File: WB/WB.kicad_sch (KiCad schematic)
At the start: 30 parts, among them J1 Conn_01x04, J2 Conn_01x04, J3 Conn_01x04, J4 Screw_Terminal_01x02, Q1 Q_NMOS_GDS, Q2 Q_NMOS_GDS, Q3 Q_NMOS_GDS, Q4 Q_NMOS_GDS, Q5 Q_NMOS_GDS, Q6 Q_NPN_ECB, SW1 SW_DIP_x06, U1 74HC165, U2 74HC595

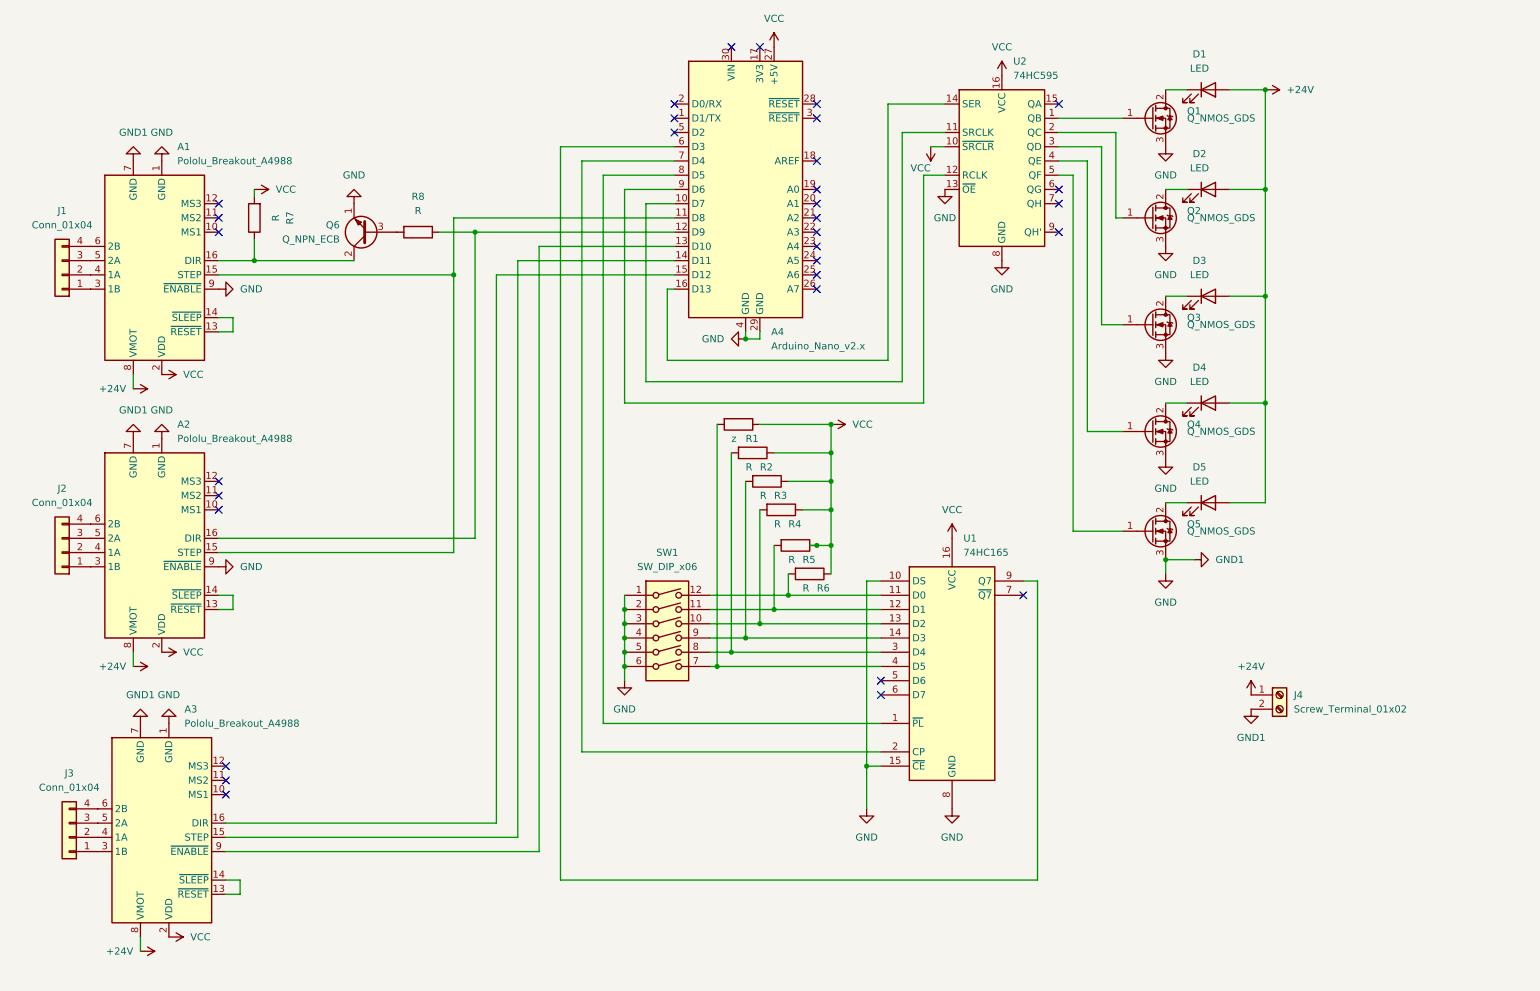
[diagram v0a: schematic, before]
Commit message: ファン、アクチュエーターを追加。配置を修正
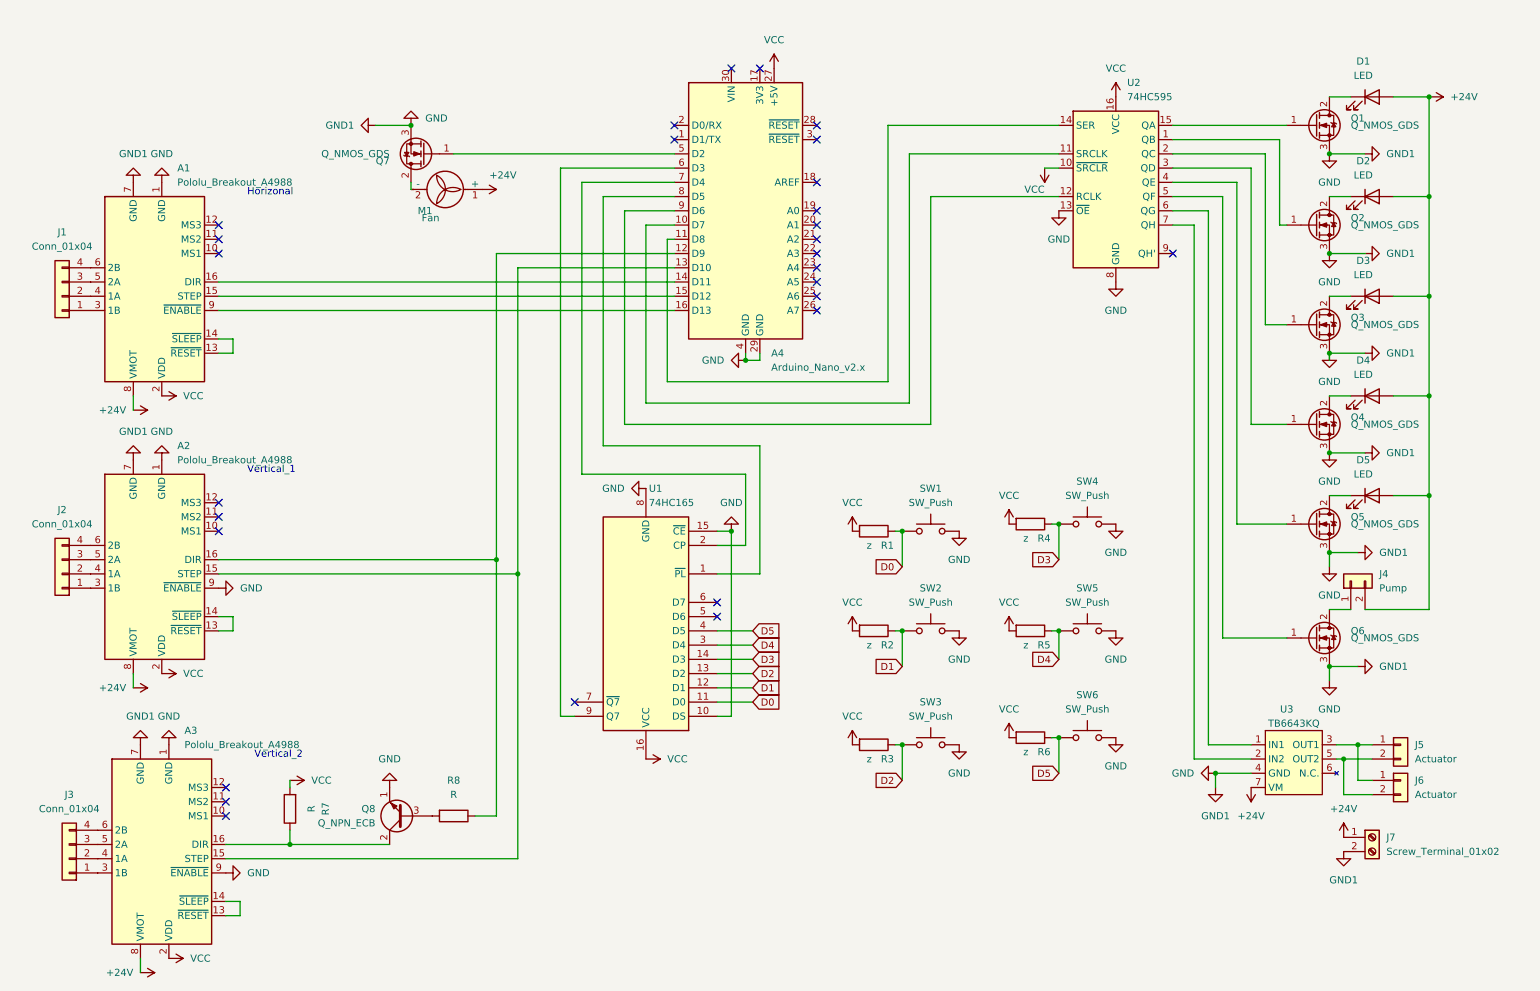
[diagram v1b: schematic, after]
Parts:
- removed Q6: Q_NPN_ECB, Package_TO_SOT_THT:TO-92_Inline, symbol Device:Q_NPN_ECB
- removed SW1: SW_DIP_x06, Connector_PinHeader_2.00mm:PinHeader_2x06_P2.00mm_Vertical, symbol Switch:SW_DIP_x06
- added J4: Pump, Connector_PinHeader_1.27mm:PinHeader_1x02_P1.27mm_Vertical, symbol Connector_Generic:Conn_01x02
- added J5, J6: Actuator, Connector_PinHeader_1.27mm:PinHeader_1x02_P1.27mm_Vertical, symbol Connector_Generic:Conn_01x02
- added M1: Fan, Connector_PinHeader_1.27mm:PinHeader_1x02_P1.27mm_Vertical, symbol Motor:Fan
- added Q6, Q7: Q_NMOS_GDS, 2sk2232:TO254P1054X470X1955-3, symbol Device:Q_NMOS_GDS
- added Q8: Q_NPN_ECB, Package_TO_SOT_THT:TO-92_Inline, symbol Device:Q_NPN_ECB
- added SW1, SW2, SW3, SW4, SW5, SW6: SW_Push, Connector_PinHeader_1.27mm:PinHeader_1x02_P1.27mm_Vertical, symbol Switch:SW_Push
- added U3: TB6643KQ, TB6643KQ:SIP1005W50P254L1965H1265Q7, symbol TB6643KQ:TB6643KQ
- D1, D2, D3, D4, D5: footprint LED_THT:LED_D10.0mm -> Connector_PinHeader_1.27mm:PinHeader_1x02_P1.27mm_Vertical
- Q1, Q2, Q3, Q4, Q5: footprint 2k2232:TO254P1054X470X1955-3 -> 2sk2232:TO254P1054X470X1955-3
- R2, R3, R4, R5, R6: value R -> z
- renumbered J4 to J7
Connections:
- net +24V: now also J4.2 (Pin_2), M1.1 (+), U3.7 (VM)
- net GND: now also A3.9 (~{ENABLE}), Q6.3 (S), Q7.3 (S), Q8.1 (E), SW1.2, SW2.2, SW3.2, SW4.2, SW5.2, SW6.2, U3.4 (GND); no longer A1.9 (~{ENABLE})
- net VCC: now also R1.2, R2.2, R3.2, R4.2, R5.2, R6.2; no longer R1.1, R2.1, R3.1, R4.1, R5.1, R6.1
- net at A3.15 (STEP): now also A2.15 (STEP), A4.13 (D10); no longer A4.14 (D11)
- net at A3.16 (DIR): now also R7.1, Q8.2 (C); no longer A4.15 (D12)
- net at Q1.1 (G): now also U2.15 (QA); no longer U2.1 (QB)
- net at Q5.1 (G): now also U2.4 (QE); no longer U2.5 (QF)
- net D2: now reaches U1.13 (D2)
- net D2: now also R3.1, SW3.1; no longer R4.2
- net D1: now reaches U1.12 (D1)
- net D1: now also R2.1, SW2.1; no longer R5.2
- net D0: now reaches U1.11 (D0)
- net D0: now also R1.1, SW1.1; no longer R6.2
- net D5: now reaches U1.4 (D5)
- net D5: now also R6.1, SW6.1; no longer R1.2
- net D4: now reaches U1.3 (D4)
- net D4: now also R5.1, SW5.1; no longer R2.2
- net D3: now reaches U1.14 (D3)
- net D3: now also R4.1, SW4.1; no longer R3.2
- net at U2.14 (SER): now also A4.11 (D8); no longer A4.16 (D13)
- net at A4.5 (D2): now also Q7.1 (G)
- net at R8.2: now also Q8.3 (B)
- net at A1.16 (DIR): now also A4.14 (D11); no longer R7.1
- net at Q3.1 (G): now also U2.2 (QC); no longer U2.3 (QD)
- net at Q2.1 (G): now also U2.1 (QB); no longer U2.2 (QC)
- net at Q4.1 (G): now also U2.3 (QD); no longer U2.4 (QE)
- net at U2.6 (QG): now also U3.1 (IN1)
- net at U2.7 (QH): now also U3.2 (IN2)
- new net: A1.15 (STEP), A4.15 (D12)
- new net: A1.9 (~{ENABLE}), A4.16 (D13)
- new net: J5.1 (Pin_1), J6.1 (Pin_1), U3.3 (OUT1)
- new net: J5.2 (Pin_2), J6.2 (Pin_2), U3.5 (OUT2)
- new net: J4.1 (Pin_1), Q6.2 (D)
- new net: M1.2 (-), Q7.2 (D)
- new net: Q6.1 (G), U2.5 (QF)
- no-connect marks 32 -> 28
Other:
- note added: "Horizonal"
- note added: "Vertical_1"
- note added: "Vertical_2"
- moved on the sheet: A1, A2, A3, A4, D1, D2, D3, D4, D5, J1, J2, J3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

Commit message: 配線の修正
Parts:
- added J1: Conn_01x04, Connector_PinHeader_2.54mm:PinHeader_1x04_P2.54mm_Vertical, symbol Connector_Generic:Conn_01x04
- renumbered J1 to J2, J2 to J3, J3 to J4, J4 to J5, J5 to J6, J6 to J7, J7 to J8
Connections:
- net at A1.3 (1B), J2.1 (Pin_1): now also J1.1 (Pin_1)
- net at A1.4 (1A), J2.2 (Pin_2): now also J1.2 (Pin_2)
- net at A1.5 (2A), J2.3 (Pin_3): now also J1.3 (Pin_3)
- net at A1.6 (2B), J2.4 (Pin_4): now also J1.4 (Pin_4)
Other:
- moved on the sheet: A1, A2, A3, J2, J3, J4

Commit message: ICのDIPを変更。
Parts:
- U1, U2: footprint Package_DIP:DIP-16_W10.16mm -> Package_DIP:DIP-16_W7.62mm
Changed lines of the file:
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@@
       (effects (font (size 1.27 1.27)) (justify left))
     )
-    (property "Footprint" "Package_DIP:DIP-16_W10.16mm" (id 2) (at 210.82 39.37 0)
+    (property "Footprint" "Package_DIP:DIP-16_W7.62mm" (id 2) (at 210.82 39.37 0)
       (effects (font (size 1.27 1.27)) hide)
     )
@@
       (effects (font (size 1.27 1.27)) (justify right))
     )
-    (property "Footprint" "Package_DIP:DIP-16_W10.16mm" (id 2) (at 127 119.38 0)
+    (property "Footprint" "Package_DIP:DIP-16_W7.62mm" (id 2) (at 127 119.38 0)
       (effects (font (size 1.27 1.27)) hide)
     )
@@
     )
     (path "/eb779460-b2c1-42b6-8c85-0417c0d93c62"
-      (reference "U1") (unit 1) (value "74HC165") (footprint "Package_DIP:DIP-16_W10.16mm")
+      (reference "U1") (unit 1) (value "74HC165") (footprint "Package_DIP:DIP-16_W7.62mm")
     )
     (path "/921a3599-130b-432e-842b-41d3a9775a60"
-      (reference "U2") (unit 1) (value "74HC595") (footprint "Package_DIP:DIP-16_W10.16mm")
+      (reference "U2") (unit 1) (value "74HC595") (footprint "Package_DIP:DIP-16_W7.62mm")
     )
     (path "/4e6330dc-1802-420a-9254-c49dd9898d9e"

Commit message: 配線がかぶっていたところを修正
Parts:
- J5, J6, J7, SW1, SW2, SW3, SW4, SW5, SW6: footprint Connector_PinHeader_1.27mm:PinHeader_1x02_P1.27mm_Vertical -> Connector_PinHeader_2.54mm:PinHeader_1x02_P2.54mm_Vertical
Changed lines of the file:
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@@
     (property "Reference" "SW6" (id 0) (at 205.74 130.81 0))
     (property "Value" "SW_Push" (id 1) (at 205.74 133.35 0))
-    (property "Footprint" "Connector_PinHeader_1.27mm:PinHeader_1x02_P1.27mm_Vertical" (id 2) (at 205.74 133.35 0)
+    (property "Footprint" "Connector_PinHeader_2.54mm:PinHeader_1x02_P2.54mm_Vertical" (id 2) (at 205.74 133.35 0)
       (effects (font (size 1.27 1.27)) hide)
     )
@@
     (property "Reference" "SW3" (id 0) (at 177.8 132.08 0))
     (property "Value" "SW_Push" (id 1) (at 177.8 134.62 0))
-    (property "Footprint" "Connector_PinHeader_1.27mm:PinHeader_1x02_P1.27mm_Vertical" (id 2) (at 177.8 134.62 0)
+    (property "Footprint" "Connector_PinHeader_2.54mm:PinHeader_1x02_P2.54mm_Vertical" (id 2) (at 177.8 134.62 0)
       (effects (font (size 1.27 1.27)) hide)
     )
@@
       (effects (font (size 1.27 1.27)) (justify right))
     )
-    (property "Footprint" "Connector_PinHeader_1.27mm:PinHeader_1x02_P1.27mm_Vertical" (id 2) (at 252.73 110.49 0)
+    (property "Footprint" "Connector_PinHeader_2.54mm:PinHeader_1x02_P2.54mm_Vertical" (id 2) (at 252.73 110.49 0)
       (effects (font (size 1.27 1.27)) hide)
     )
@@
     (property "Reference" "SW5" (id 0) (at 205.74 111.76 0))
     (property "Value" "SW_Push" (id 1) (at 205.74 114.3 0))
-    (property "Footprint" "Connector_PinHeader_1.27mm:PinHeader_1x02_P1.27mm_Vertical" (id 2) (at 205.74 114.3 0)
+    (property "Footprint" "Connector_PinHeader_2.54mm:PinHeader_1x02_P2.54mm_Vertical" (id 2) (at 205.74 114.3 0)
       (effects (font (size 1.27 1.27)) hide)
     )
@@
     (property "Reference" "SW1" (id 0) (at 177.8 93.98 0))
     (property "Value" "SW_Push" (id 1) (at 177.8 96.52 0))
-    (property "Footprint" "Connector_PinHeader_1.27mm:PinHeader_1x02_P1.27mm_Vertical" (id 2) (at 177.8 96.52 0)
+    (property "Footprint" "Connector_PinHeader_2.54mm:PinHeader_1x02_P2.54mm_Vertical" (id 2) (at 177.8 96.52 0)
       (effects (font (size 1.27 1.27)) hide)
     )
@@
       (effects (font (size 1.27 1.27)) (justify left))
     )
-    (property "Footprint" "Connector_PinHeader_1.27mm:PinHeader_1x02_P1.27mm_Vertical" (id 2) (at 261.62 146.05 0)
+    (property "Footprint" "Connector_PinHeader_2.54mm:PinHeader_1x02_P2.54mm_Vertical" (id 2) (at 261.62 146.05 0)
       (effects (font (size 1.27 1.27)) hide)
     )
@@
     (property "Reference" "SW2" (id 0) (at 177.8 111.76 0))
     (property "Value" "SW_Push" (id 1) (at 177.8 114.3 0))
-    (property "Footprint" "Connector_PinHeader_1.27mm:PinHeader_1x02_P1.27mm_Vertical" (id 2) (at 177.8 114.3 0)
+    (property "Footprint" "Connector_PinHeader_2.54mm:PinHeader_1x02_P2.54mm_Vertical" (id 2) (at 177.8 114.3 0)
       (effects (font (size 1.27 1.27)) hide)
     )
@@
     (property "Reference" "SW4" (id 0) (at 205.74 92.71 0))
     (property "Value" "SW_Push" (id 1) (at 205.74 95.25 0))
-    (property "Footprint" "Connector_PinHeader_1.27mm:PinHeader_1x02_P1.27mm_Vertical" (id 2) (at 205.74 95.25 0)
+    (property "Footprint" "Connector_PinHeader_2.54mm:PinHeader_1x02_P2.54mm_Vertical" (id 2) (at 205.74 95.25 0)
       (effects (font (size 1.27 1.27)) hide)
     )
@@
       (effects (font (size 1.27 1.27)) (justify left))
     )
-    (property "Footprint" "Connector_PinHeader_1.27mm:PinHeader_1x02_P1.27mm_Vertical" (id 2) (at 261.62 139.7 0)
+    (property "Footprint" "Connector_PinHeader_2.54mm:PinHeader_1x02_P2.54mm_Vertical" (id 2) (at 261.62 139.7 0)
       (effects (font (size 1.27 1.27)) hide)
     )
@@
     )
     (path "/4ff7670f-d345-4c37-b0b9-abc60cb59b1a"
-      (reference "J5") (unit 1) (value "Pump") (footprint "Connector_PinHeader_1.27mm:PinHeader_1x02_P1.27mm_Vertical")
+      (reference "J5") (unit 1) (value "Pump") (footprint "Connector_PinHeader_2.54mm:PinHeader_1x02_P2.54mm_Vertical")
     )
     (path "/cac0fc0e-cec6-4b33-9d69-c0f864593a0b"
-      (reference "J6") (unit 1) (value "Actuator") (footprint "Connector_PinHeader_1.27mm:PinHeader_1x02_P1.27mm_Vertical")
+      (reference "J6") (unit 1) (value "Actuator") (footprint "Connector_PinHeader_2.54mm:PinHeader_1x02_P2.54mm_Vertical")
     )
     (path "/8c033d7a-9f0a-40df-a3a8-cdccfee65698"
-      (reference "J7") (unit 1) (value "Actuator") (footprint "Connector_PinHeader_1.27mm:PinHeader_1x02_P1.27mm_Vertical")
+      (reference "J7") (unit 1) (value "Actuator") (footprint "Connector_PinHeader_2.54mm:PinHeader_1x02_P2.54mm_Vertical")
     )
     (path "/211b8208-cbdb-4b93-9929-98fb36f4e4ff"
@@
     )
     (path "/7c141a6e-f956-46e0-b692-50e3d9a9e88e"
-      (reference "SW1") (unit 1) (value "SW_Push") (footprint "Connector_PinHeader_1.27mm:PinHeader_1x02_P1.27mm_Vertical")
+      (reference "SW1") (unit 1) (value "SW_Push") (footprint "Connector_PinHeader_2.54mm:PinHeader_1x02_P2.54mm_Vertical")
     )
     (path "/c081e0d4-4bbe-425c-a1aa-52b71abf8704"
-      (reference "SW2") (unit 1) (value "SW_Push") (footprint "Connector_PinHeader_1.27mm:PinHeader_1x02_P1.27mm_Vertical")
+      (reference "SW2") (unit 1) (value "SW_Push") (footprint "Connector_PinHeader_2.54mm:PinHeader_1x02_P2.54mm_Vertical")
     )
     (path "/4a62376c-2bb0-4bce-bca0-efedd85984e1"
-      (reference "SW3") (unit 1) (value "SW_Push") (footprint "Connector_PinHeader_1.27mm:PinHeader_1x02_P1.27mm_Vertical")
+      (reference "SW3") (unit 1) (value "SW_Push") (footprint "Connector_PinHeader_2.54mm:PinHeader_1x02_P2.54mm_Vertical")
     )
     (path "/c9768221-a320-4dce-bd3c-a7275cf441e4"
-      (reference "SW4") (unit 1) (value "SW_Push") (footprint "Connector_PinHeader_1.27mm:PinHeader_1x02_P1.27mm_Vertical")
+      (reference "SW4") (unit 1) (value "SW_Push") (footprint "Connector_PinHeader_2.54mm:PinHeader_1x02_P2.54mm_Vertical")
     )
     (path "/68261210-529f-4e53-b490-8e8571204e46"
-      (reference "SW5") (unit 1) (value "SW_Push") (footprint "Connector_PinHeader_1.27mm:PinHeader_1x02_P1.27mm_Vertical")
+      (reference "SW5") (unit 1) (value "SW_Push") (footprint "Connector_PinHeader_2.54mm:PinHeader_1x02_P2.54mm_Vertical")
     )
     (path "/3fedebd7-15cf-4483-a3e2-abad3c1b862c"
-      (reference "SW6") (unit 1) (value "SW_Push") (footprint "Connector_PinHeader_1.27mm:PinHeader_1x02_P1.27mm_Vertical")
+      (reference "SW6") (unit 1) (value "SW_Push") (footprint "Connector_PinHeader_2.54mm:PinHeader_1x02_P2.54mm_Vertical")
     )
     (path "/eb779460-b2c1-42b6-8c85-0417c0d93c62"

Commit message: パッドのサイズを変更したが、だめ
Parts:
- D1, D2, D3, D4, D5, M1: footprint Connector_PinHeader_1.27mm:PinHeader_1x02_P1.27mm_Vertical -> Connector_PinHeader_2.54mm:PinHeader_1x02_P2.54mm_Vertical
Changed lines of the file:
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@@
     (property "Reference" "D2" (id 0) (at 254.9525 35.56 0))
     (property "Value" "LED" (id 1) (at 254.9525 38.1 0))
-    (property "Footprint" "Connector_PinHeader_1.27mm:PinHeader_1x02_P1.27mm_Vertical" (id 2) (at 256.54 41.91 0)
+    (property "Footprint" "Connector_PinHeader_2.54mm:PinHeader_1x02_P2.54mm_Vertical" (id 2) (at 256.54 41.91 0)
       (effects (font (size 1.27 1.27)) hide)
     )
@@
     (property "Reference" "D1" (id 0) (at 254.9525 17.78 0))
     (property "Value" "LED" (id 1) (at 254.9525 20.32 0))
-    (property "Footprint" "Connector_PinHeader_1.27mm:PinHeader_1x02_P1.27mm_Vertical" (id 2) (at 256.54 24.13 0)
+    (property "Footprint" "Connector_PinHeader_2.54mm:PinHeader_1x02_P2.54mm_Vertical" (id 2) (at 256.54 24.13 0)
       (effects (font (size 1.27 1.27)) hide)
     )
@@
     (property "Reference" "D5" (id 0) (at 254.9525 88.9 0))
     (property "Value" "LED" (id 1) (at 254.9525 91.44 0))
-    (property "Footprint" "Connector_PinHeader_1.27mm:PinHeader_1x02_P1.27mm_Vertical" (id 2) (at 256.54 95.25 0)
+    (property "Footprint" "Connector_PinHeader_2.54mm:PinHeader_1x02_P2.54mm_Vertical" (id 2) (at 256.54 95.25 0)
       (effects (font (size 1.27 1.27)) hide)
     )
@@
     (property "Reference" "D4" (id 0) (at 254.9525 71.12 0))
     (property "Value" "LED" (id 1) (at 254.9525 73.66 0))
-    (property "Footprint" "Connector_PinHeader_1.27mm:PinHeader_1x02_P1.27mm_Vertical" (id 2) (at 256.54 77.47 0)
+    (property "Footprint" "Connector_PinHeader_2.54mm:PinHeader_1x02_P2.54mm_Vertical" (id 2) (at 256.54 77.47 0)
       (effects (font (size 1.27 1.27)) hide)
     )
@@
       (effects (font (size 1.27 1.27)) (justify right))
     )
-    (property "Footprint" "Connector_PinHeader_1.27mm:PinHeader_1x02_P1.27mm_Vertical" (id 2) (at 90.424 40.64 0)
+    (property "Footprint" "Connector_PinHeader_2.54mm:PinHeader_1x02_P2.54mm_Vertical" (id 2) (at 90.424 40.64 0)
       (effects (font (size 1.27 1.27)) hide)
     )
@@
     (property "Reference" "D3" (id 0) (at 254.9525 53.34 0))
     (property "Value" "LED" (id 1) (at 254.9525 55.88 0))
-    (property "Footprint" "Connector_PinHeader_1.27mm:PinHeader_1x02_P1.27mm_Vertical" (id 2) (at 256.54 59.69 0)
+    (property "Footprint" "Connector_PinHeader_2.54mm:PinHeader_1x02_P2.54mm_Vertical" (id 2) (at 256.54 59.69 0)
       (effects (font (size 1.27 1.27)) hide)
     )
@@
     )
     (path "/33f74c42-df09-4e7f-8b9f-aead0e84dbd8"
-      (reference "D1") (unit 1) (value "LED") (footprint "Connector_PinHeader_1.27mm:PinHeader_1x02_P1.27mm_Vertical")
+      (reference "D1") (unit 1) (value "LED") (footprint "Connector_PinHeader_2.54mm:PinHeader_1x02_P2.54mm_Vertical")
     )
     (path "/1b324149-b8e8-46ba-b558-a0b7e606372c"
-      (reference "D2") (unit 1) (value "LED") (footprint "Connector_PinHeader_1.27mm:PinHeader_1x02_P1.27mm_Vertical")
+      (reference "D2") (unit 1) (value "LED") (footprint "Connector_PinHeader_2.54mm:PinHeader_1x02_P2.54mm_Vertical")
     )
     (path "/bca4d978-cbcd-4643-8e6a-dad0d5679eca"
-      (reference "D3") (unit 1) (value "LED") (footprint "Connector_PinHeader_1.27mm:PinHeader_1x02_P1.27mm_Vertical")
+      (reference "D3") (unit 1) (value "LED") (footprint "Connector_PinHeader_2.54mm:PinHeader_1x02_P2.54mm_Vertical")
     )
     (path "/64f8dc80-9614-44d9-8d0d-8398eec9622d"
-      (reference "D4") (unit 1) (value "LED") (footprint "Connector_PinHeader_1.27mm:PinHeader_1x02_P1.27mm_Vertical")
+      (reference "D4") (unit 1) (value "LED") (footprint "Connector_PinHeader_2.54mm:PinHeader_1x02_P2.54mm_Vertical")
     )
     (path "/54397674-6d80-4017-bf5d-4afd9f92cf6d"
-      (reference "D5") (unit 1) (value "LED") (footprint "Connector_PinHeader_1.27mm:PinHeader_1x02_P1.27mm_Vertical")
+      (reference "D5") (unit 1) (value "LED") (footprint "Connector_PinHeader_2.54mm:PinHeader_1x02_P2.54mm_Vertical")
     )
     (path "/a3885859-56b0-42a3-8958-3267b16ee289"
@@
     )
     (path "/9dce8f72-5a73-4c40-9128-1e8384168005"
-      (reference "M1") (unit 1) (value "Fan") (footprint "Connector_PinHeader_1.27mm:PinHeader_1x02_P1.27mm_Vertical")
+      (reference "M1") (unit 1) (value "Fan") (footprint "Connector_PinHeader_2.54mm:PinHeader_1x02_P2.54mm_Vertical")
     )
     (path "/0e74d2d6-1619-4a74-b9d8-b5bffdc93d16"
